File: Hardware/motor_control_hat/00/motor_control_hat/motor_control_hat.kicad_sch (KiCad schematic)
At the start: 32 parts, among them P1 TB_1x2_5.08mm_RA, P10 X9254WR-04-N0SN, P11 X9254WR-04-N0SN, P12 X9254WR-04-N0SN, P13 X9254WR-04-N0SN, P2 TB_1x2_5.08mm_RA, P3 TB_1x2_5.08mm_RA, P4 TB_1x2_5.08mm_RA, P5 X9254WR-04-N0SN, P6 X9254WR-04-N0SN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

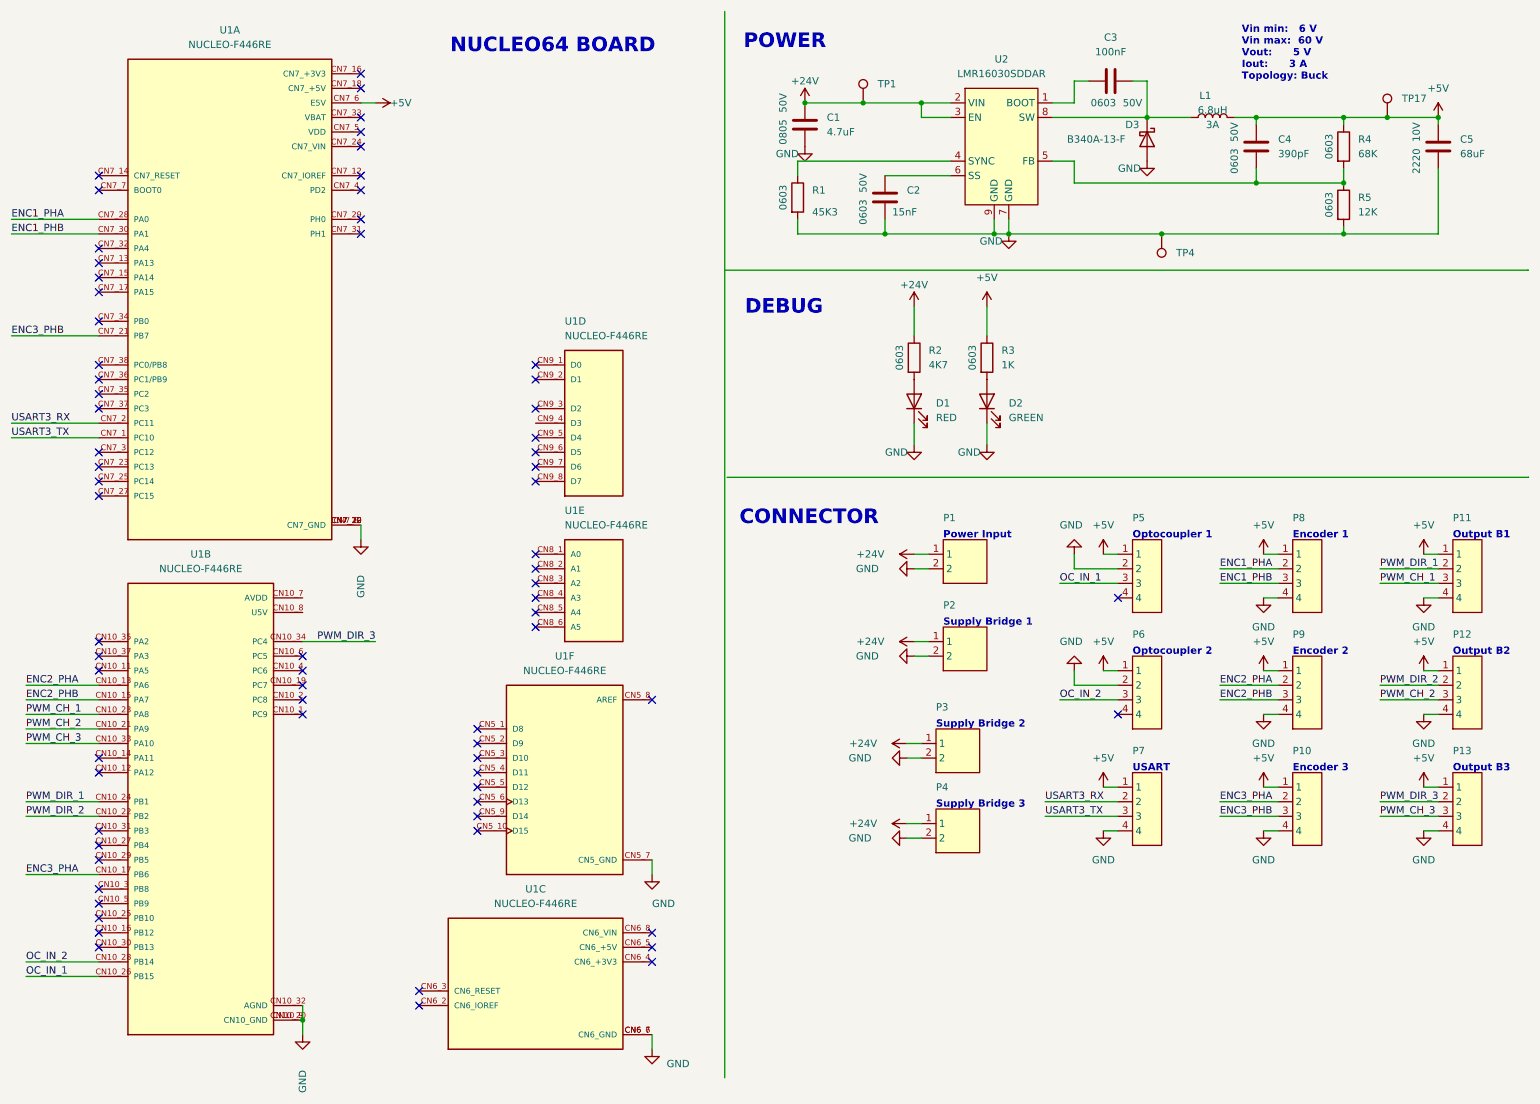
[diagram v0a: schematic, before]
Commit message: Motor hat V0 created
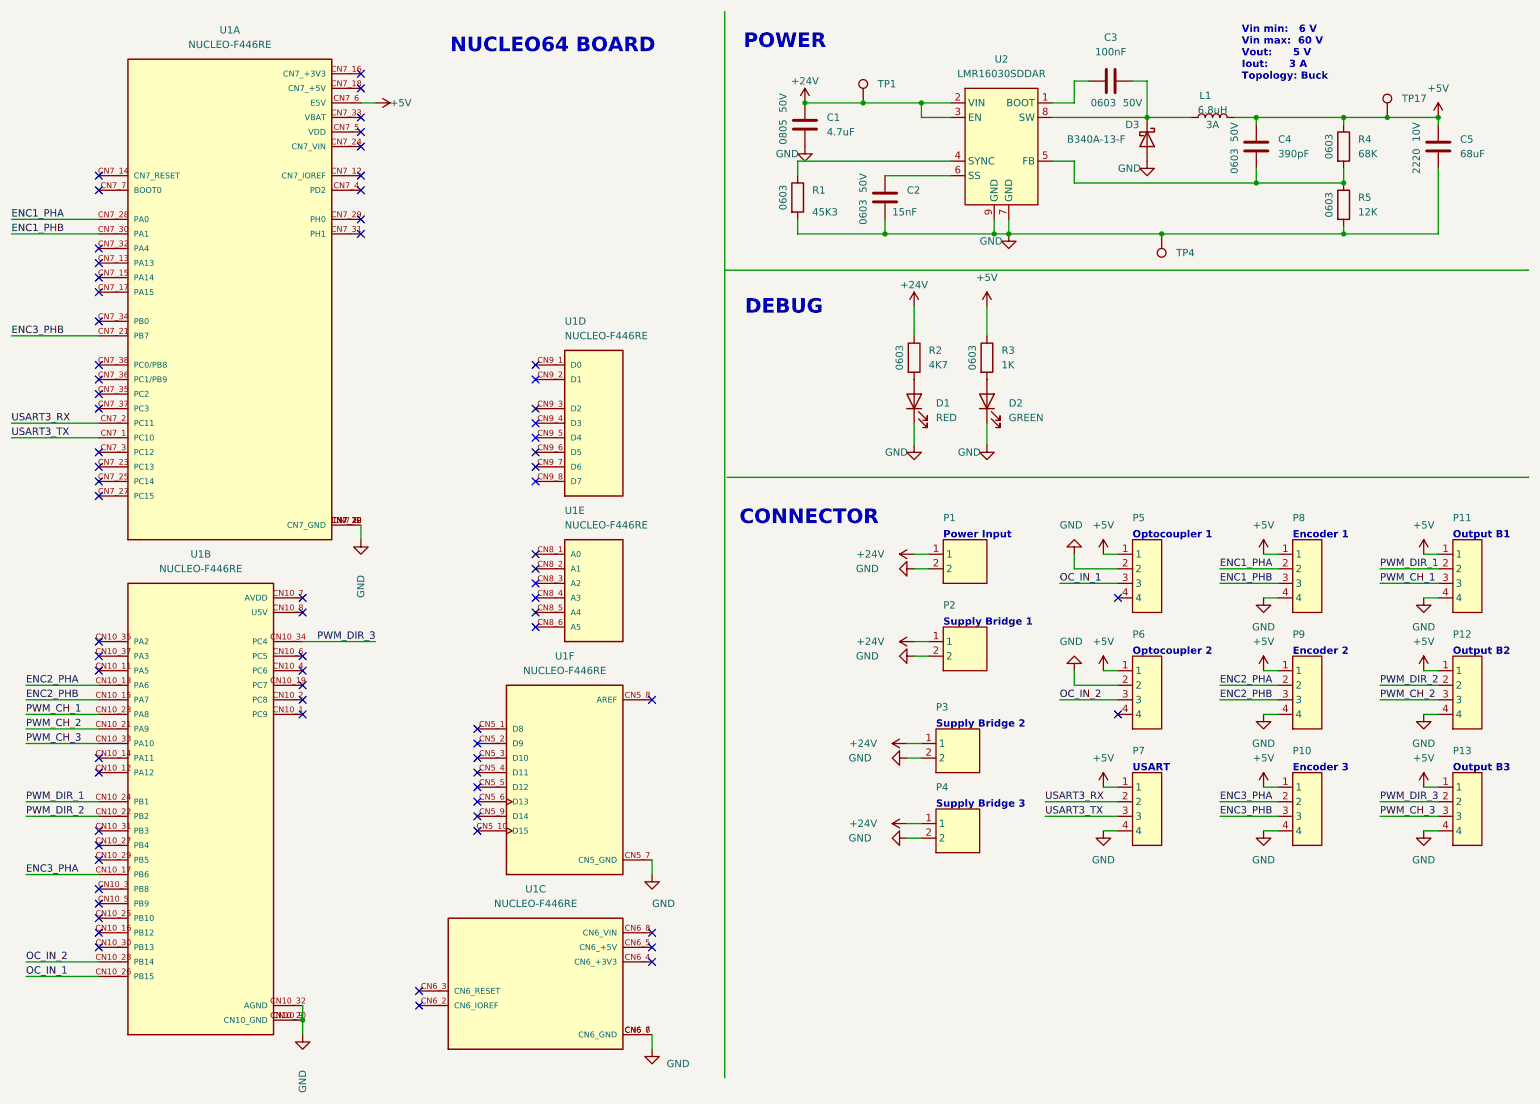
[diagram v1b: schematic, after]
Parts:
- TP1, TP17, TP4: now left out of the parts list
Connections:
- no-connect marks 71 -> 74
